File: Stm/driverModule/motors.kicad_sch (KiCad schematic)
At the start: 27 parts, among them J1 Conn_02x05_Odd_Even, J202 Conn_01x04_Pin, Q1 BSS138, Q2 BSS138, Q3 AON7410, U1 TLE94103EP, U201 DRV8838, U204 VNH5019A-E

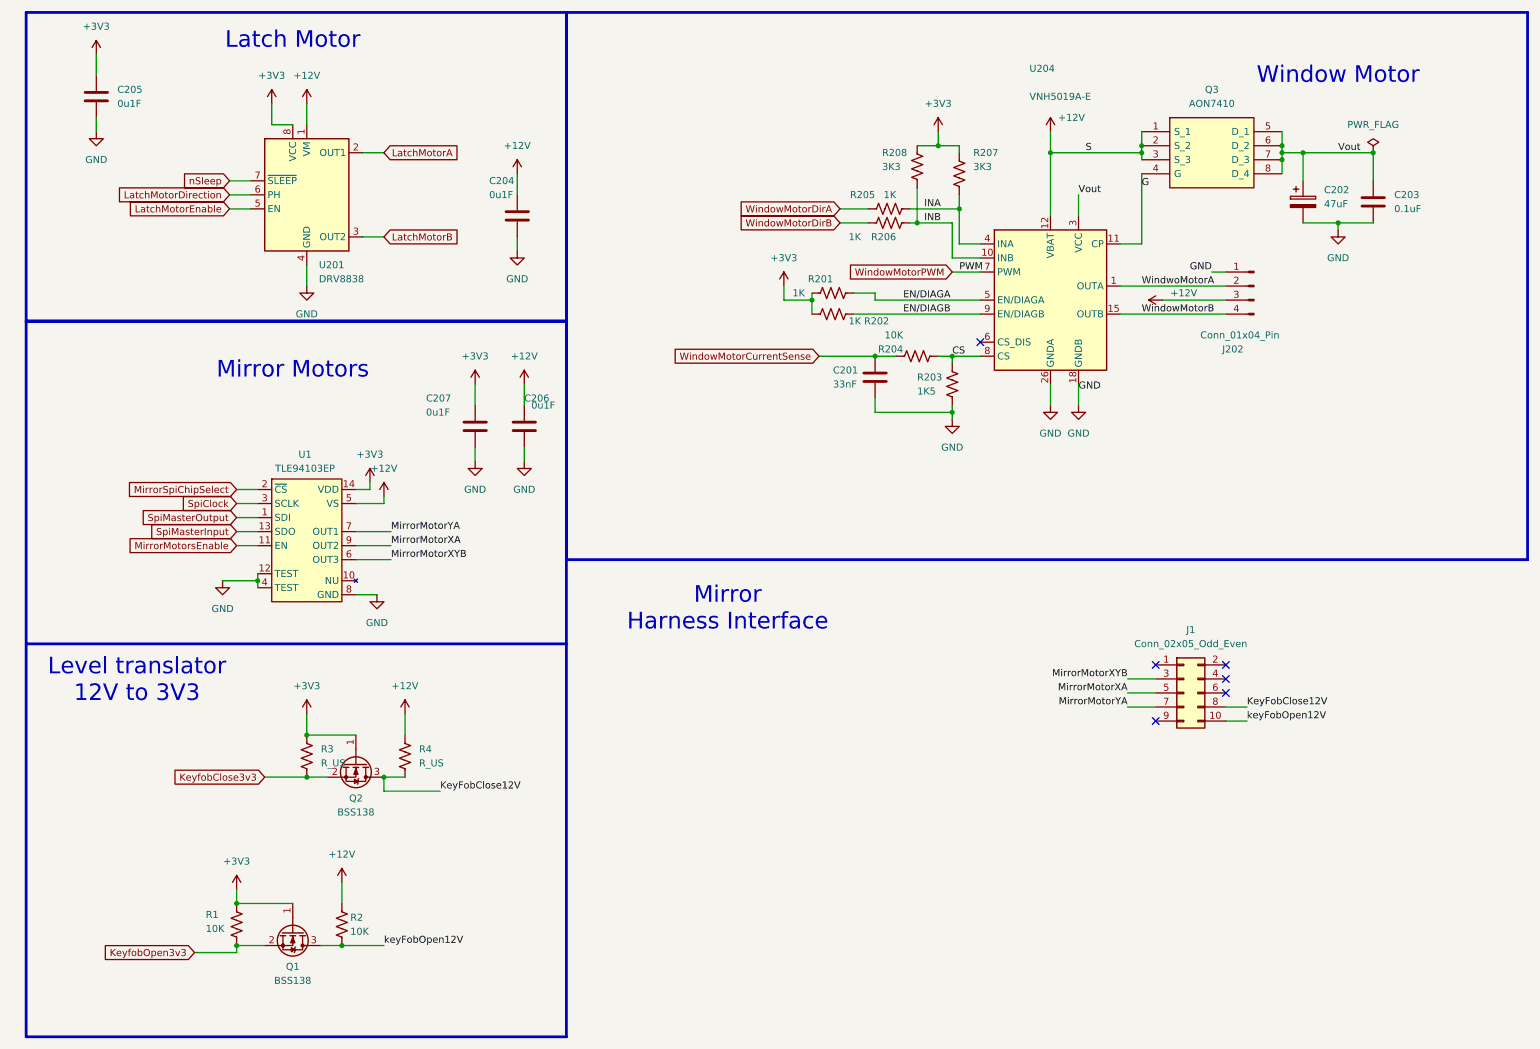
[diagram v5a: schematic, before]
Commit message: 3d Models
Added Some 3d Models
And remove some components from schematic
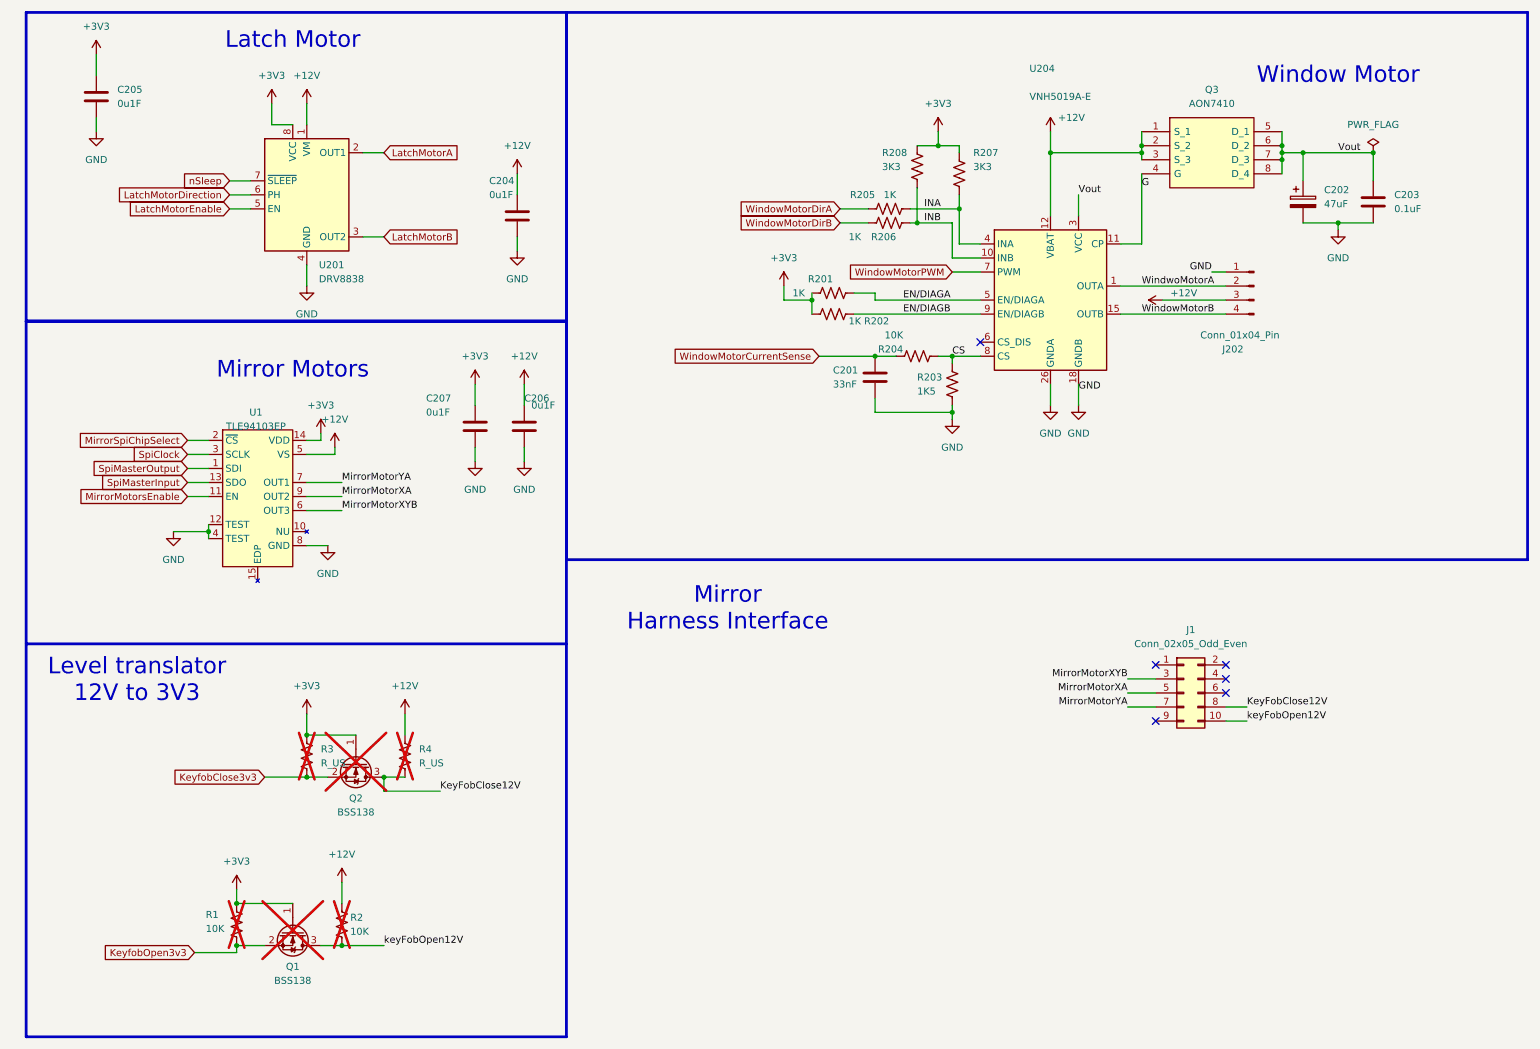
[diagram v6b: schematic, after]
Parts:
- C203, C204, C205, C206, C207: footprint (none) -> Capacitor_SMD:C_0402_1005Metric_Pad0.74x0.62mm_HandSolder
- Q1, Q2, R1, R2, R3, R4: now not fitted

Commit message: Changed Connector
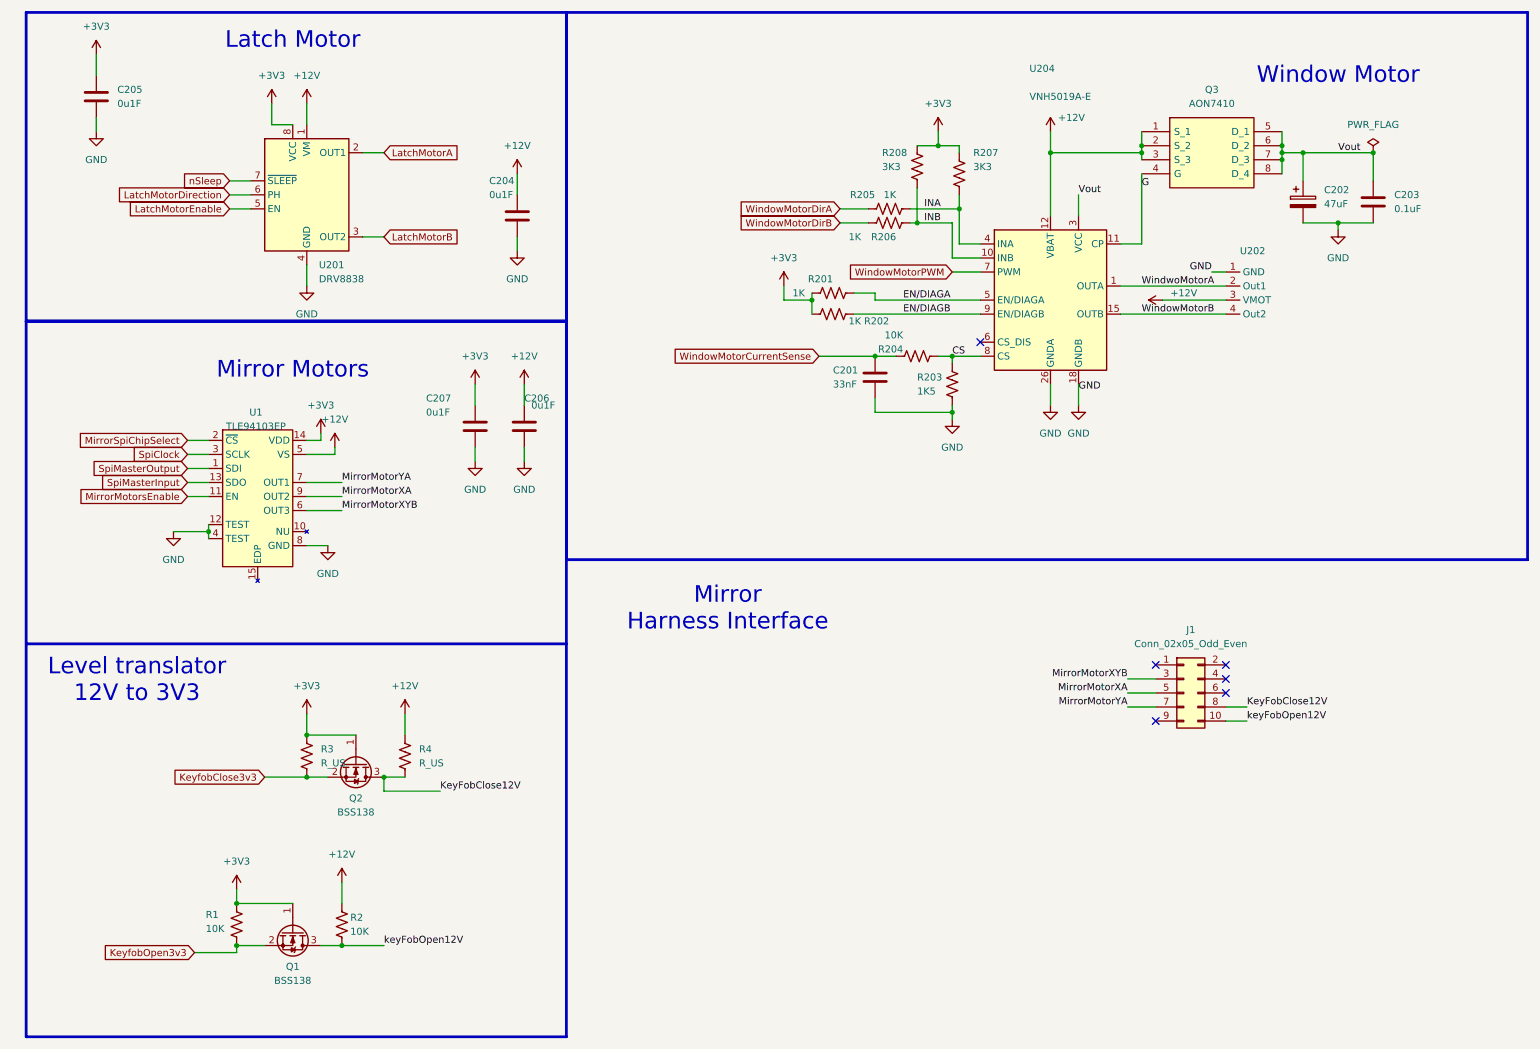
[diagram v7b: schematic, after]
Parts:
- removed J202: Conn_01x04_Pin, Connector_Phoenix_MC_HighVoltage:PhoenixContact_MCV_1,5_4-G-5.08_1x04_P5.08mm_Vertical, symbol Connector:Conn_01x04_Pin
- added U202: ~, symbol Local_symbols:HeaderForCustomMotorConnector
- Q1, Q2, R1, R2, R3, R4: now fitted
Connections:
- net +12V: now also U202.3 (VMOT)
- net GND: now also U202.1 (GND)
- net WindowMotorB: now also U202.4 (Out2)
- net WindwoMotorA: now also U202.2 (Out1)
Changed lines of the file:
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@@
 	)
 	(symbol
+		(lib_id "Local_symbols:HeaderForCustomMotorConnector")
+		(at 231.14 63.5 0)
+		(unit 1)
+		(exclude_from_sim no)
+		(in_bom yes)
+		(on_board yes)
+		(dnp no)
+		(property "Reference" "U202"
+			(at 232.41 55.88 0)
+			(effects
+				(font
+					(size 1.27 1.27)
+				)
+				(justify left)
+			)
+		)
+		(property "Value" "~"
+			(at 233.68 64.77 0)
+			(effects
+				(font
+					(size 1.27 1.27)
+				)
+				(justify left)
+			)
+		)
+		(property "Footprint" ""
+			(at 232.41 62.23 0)
+			(effects
+				(font
+					(size 1.27 1.27)
+				)
+				(hide yes)
+			)
+		)
+		(property "Datasheet" ""
+			(at 232.41 62.23 0)
+			(effects
+				(font
+					(size 1.27 1.27)
+				)
+				(hide yes)
+			)
+		)
+		(property "Description" ""
+			(at 232.41 62.23 0)
+			(effects
+				(font
+					(size 1.27 1.27)
+				)
+				(hide yes)
+			)
+		)
+		(pin "3"
+		)
+		(pin "4"
+		)
+		(pin "1"
+		)
+		(pin "2"
+		)
+		(instances
+			(project ""
+				(path "/959b66be-b3e0-42f8-ad58-f1baefc5b565/929fc890-f6da-48d5-a213-781ba4c4fd4e"
+					(reference "U202")
+					(unit 1)
+				)
+			)
+		)
+	)
+	(symbol
 		(lib_id "Device:R_US")
 		(at 168.91 48.26 90)
@@
 		(exclude_from_sim no)
 		(in_bom yes)
-		(on_board no)
-		(dnp yes)
+		(on_board yes)
+		(dnp no)
 		(fields_autoplaced yes)
 		(property "Reference" "Q1"
@@
 	)
 	(symbol
-		(lib_id "Connector:Conn_01x04_Pin")
-		(at 234.95 62.23 0)
-		(mirror y)
-		(unit 1)
-		(exclude_from_sim no)
-		(in_bom yes)
-		(on_board yes)
-		(dnp no)
-		(property "Reference" "J202"
-			(at 231.14 73.66 0)
-			(effects
-				(font
-					(size 1.27 1.27)
-				)
-			)
-		)
-		(property "Value" "Conn_01x04_Pin"
-			(at 232.41 71.12 0)
-			(effects
-				(font
-					(size 1.27 1.27)
-				)
-			)
-		)
-		(property "Footprint" "Connector_Phoenix_MC_HighVoltage:PhoenixContact_MCV_1,5_4-G-5.08_1x04_P5.08mm_Vertical"
-			(at 234.95 62.23 0)
-			(effects
-				(font
-					(size 1.27 1.27)
-				)
-				(hide yes)
-			)
-		)
-		(property "Datasheet" "~"
-			(at 234.95 62.23 0)
-			(effects
-				(font
-					(size 1.27 1.27)
-				)
-				(hide yes)
-			)
-		)
-		(property "Description" "Generic connector, single row, 01x04, script generated"
-			(at 234.95 62.23 0)
-			(effects
-				(font
-					(size 1.27 1.27)
-				)
-				(hide yes)
-			)
-		)
-		(pin "2"
-		)
-		(pin "1"
-		)
-		(pin "4"
-		)
-		(pin "3"
-		)
-		(instances
-			(project ""
-				(path "/959b66be-b3e0-42f8-ad58-f1baefc5b565/929fc890-f6da-48d5-a213-781ba4c4fd4e"
-					(reference "J202")
-					(unit 1)
-				)
-			)
-		)
-	)
-	(symbol
 		(lib_id "Transistor_FET:BSS138")
 		(at 72.39 148.59 270)
@@
 		(exclude_from_sim no)
 		(in_bom yes)
-		(on_board no)
-		(dnp yes)
+		(on_board yes)
+		(dnp no)
 		(fields_autoplaced yes)
 		(property "Reference" "Q2"
@@
 		(exclude_from_sim no)
 		(in_bom yes)
-		(on_board no)
-		(dnp yes)
+		(on_board yes)
+		(dnp no)
 		(property "Reference" "R2"
 			(at 71.374 176.53 0)
@@
 		(exclude_from_sim no)
 		(in_bom yes)
-		(on_board no)
-		(dnp yes)
+		(on_board yes)
+		(dnp no)
 		(fields_autoplaced yes)
 		(property "Reference" "R3"
@@
 		(exclude_from_sim no)
 		(in_bom yes)
-		(on_board no)
-		(dnp yes)
+		(on_board yes)
+		(dnp no)
 		(fields_autoplaced yes)
 		(property "Reference" "R4"
@@
 		(exclude_from_sim no)
 		(in_bom yes)
-		(on_board no)
-		(dnp yes)
+		(on_board yes)
+		(dnp no)
 		(property "Reference" "R1"
 			(at 45.212 176.022 0)

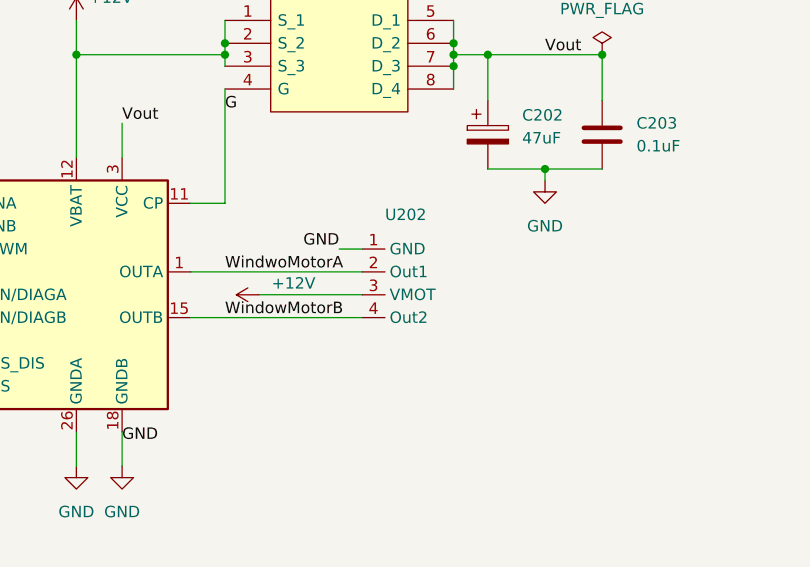
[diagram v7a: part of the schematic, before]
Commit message: PCB Board
PCB board created, need to verify connectors polarity
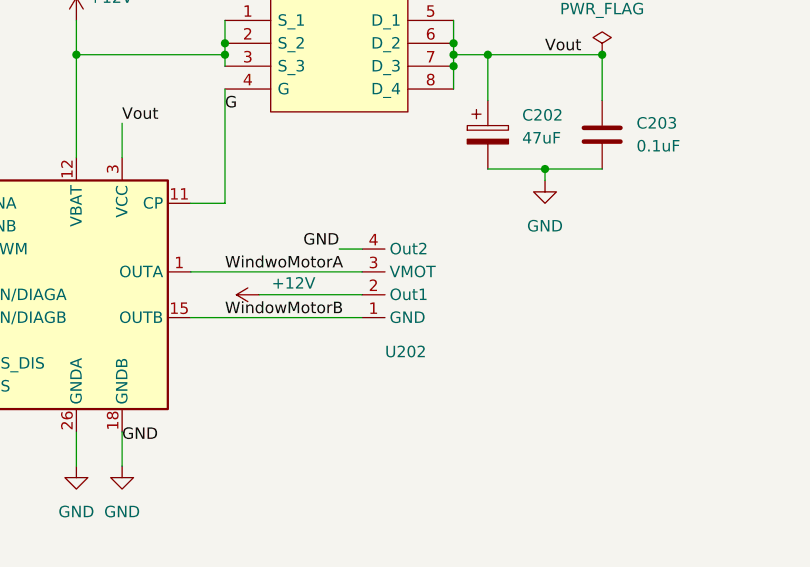
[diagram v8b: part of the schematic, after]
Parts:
- U202: footprint (none) -> Local_Footprints:HeaderMotorCustomeSMD
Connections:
- net +12V: now also U202.2 (Out1); no longer U202.3 (VMOT)
- net GND: now also U202.4 (Out2); no longer U202.1 (GND)
- net WindowMotorB: now also U202.1 (GND); no longer U202.4 (Out2)
- net WindwoMotorA: now also U202.3 (VMOT); no longer U202.2 (Out1)
